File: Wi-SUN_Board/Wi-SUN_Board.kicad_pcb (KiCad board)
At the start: 2 copper layers, 42.5 x 30 mm, 17 parts, among them J1 DF12NB_3.0_-20DS-0.5V_51_, J2 USB_C_Receptacle_USB2.0_12402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, SW1 SW_Push, U1 AP7333_33SAG_SOT23, U2 CH340E

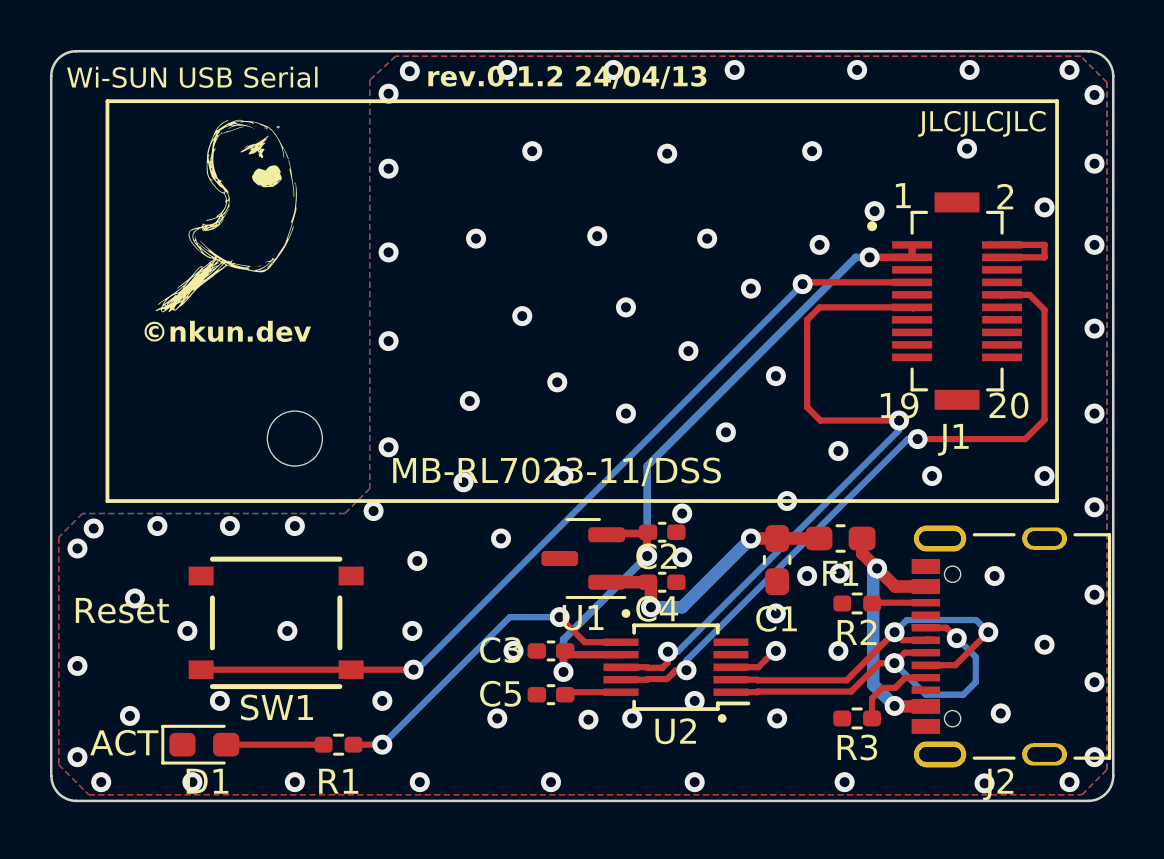
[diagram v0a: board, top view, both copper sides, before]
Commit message: フットプリントの細かい修正
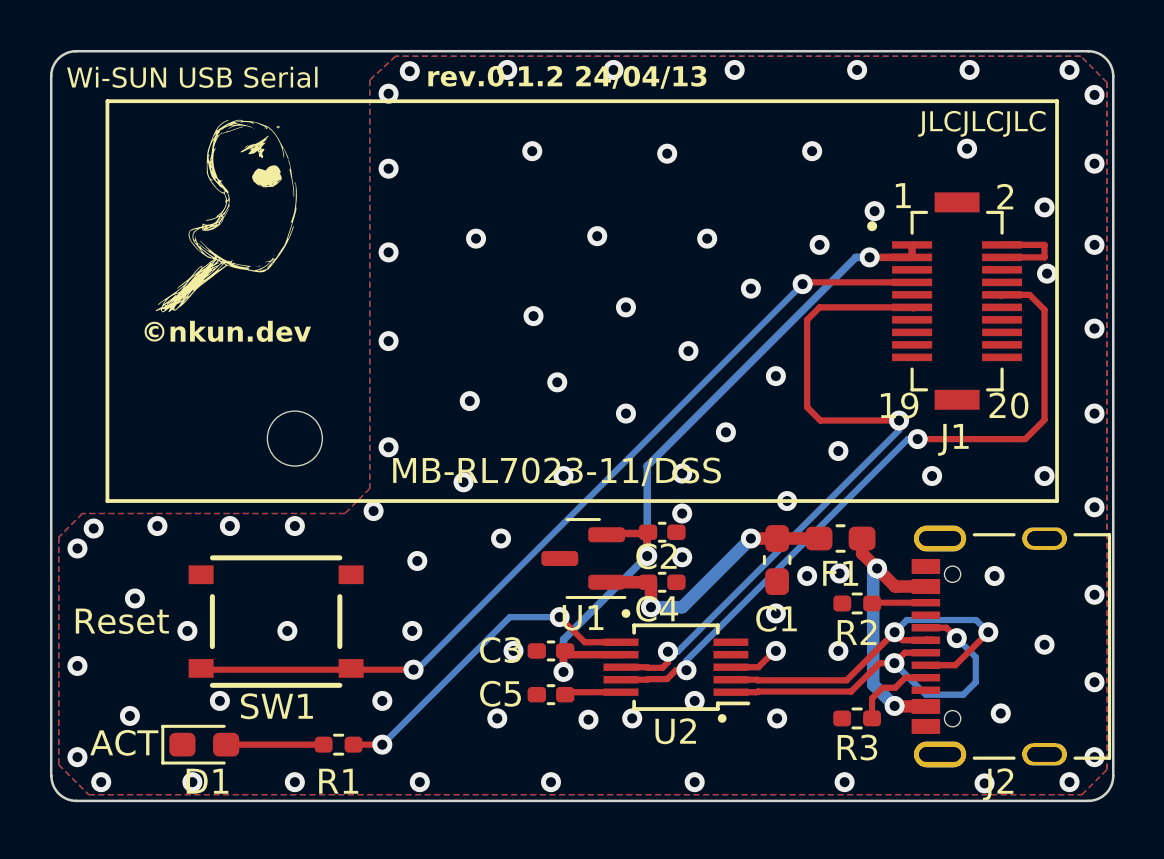
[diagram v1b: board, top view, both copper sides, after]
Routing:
- net GND: vias 88 -> 90
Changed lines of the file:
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@@
   )
   (footprint "Button_Switch_SMD:TS-1187A-B-A-B" (layer "F.Cu")
-    (at 161.75 121.875)
+    (at 161.75 121.825)
     (property "Sheetfile" "Wi-SUN_Board.kicad_sch")
     (property "Sheetname" "")
@@
     (effects (font (size 0.8 0.8) (thickness 0.125) bold) (justify left bottom))
   )
-  (gr_text "Reset\n" (at 153.6 122) (layer "F.SilkS")
+  (gr_text "Reset\n" (at 153.6 122.42675) (layer "F.SilkS")
     (effects (font (size 1 1) (thickness 0.15)) (justify left bottom))
   )
@@
   (via (at 182.2 117) (size 0.8) (drill 0.4) (layers "F.Cu" "B.Cu") (free) (net 1))
   (via (at 154.45 118.1) (size 0.8) (drill 0.4) (layers "F.Cu" "B.Cu") (free) (net 1))
+  (via (at 178 115.9) (size 0.8) (drill 0.4) (layers "F.Cu" "B.Cu") (free) (net 1))
   (via (at 153.8 118.9) (size 0.8) (drill 0.4) (layers "F.Cu" "B.Cu") (free) (net 1))
   (via (at 184.25 123) (size 0.8) (drill 0.4) (layers "F.Cu" "B.Cu") (free) (net 1))
@@
   (via (at 178 117.5) (size 0.8) (drill 0.4) (layers "F.Cu" "B.Cu") (free) (net 1))
   (via (at 159.5 125) (size 0.8) (drill 0.4) (layers "F.Cu" "B.Cu") (free) (net 1))
+  (via (at 192.6 107.9) (size 0.8) (drill 0.4) (layers "F.Cu" "B.Cu") (free) (net 1))
   (via (at 153.8 127.25) (size 0.8) (drill 0.4) (layers "F.Cu" "B.Cu") (free) (net 1))
   (via (at 181.75 121.5) (size 0.8) (drill 0.4) (layers "F.Cu" "B.Cu") (free) (net 1))
@@
   (via (at 180.75 108.5) (size 0.8) (drill 0.4) (layers "F.Cu" "B.Cu") (free) (net 1))
   (via (at 181.75 112) (size 0.8) (drill 0.4) (layers "F.Cu" "B.Cu") (free) (net 1))
-  (via (at 171.6 109.6) (size 0.8) (drill 0.4) (layers "F.Cu" "B.Cu") (free) (net 1))
+  (via (at 172.05 109.6) (size 0.8) (drill 0.4) (layers "F.Cu" "B.Cu") (free) (net 1))
   (via (at 169.5 113) (size 0.8) (drill 0.4) (layers "F.Cu" "B.Cu") (free) (net 1))
   (via (at 178.5 125) (size 0.8) (drill 0.4) (layers "F.Cu" "B.Cu") (free) (net 1))
